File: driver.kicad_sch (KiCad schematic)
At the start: 7 parts, among them J1 Conn_01x02_Pin, J2 Conn_01x02_Pin, U2 DRV8847SPWR

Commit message: patch: mark unused pins
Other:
- title: (none) -> HapticDriver
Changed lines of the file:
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@@
 	(generator_version "7.99")
 	(paper "A4")
+	(title_block
+		(title "HapticDriver")
+		(rev "v0.1")
+	)
 	(junction
 		(at 160.02 114.3)

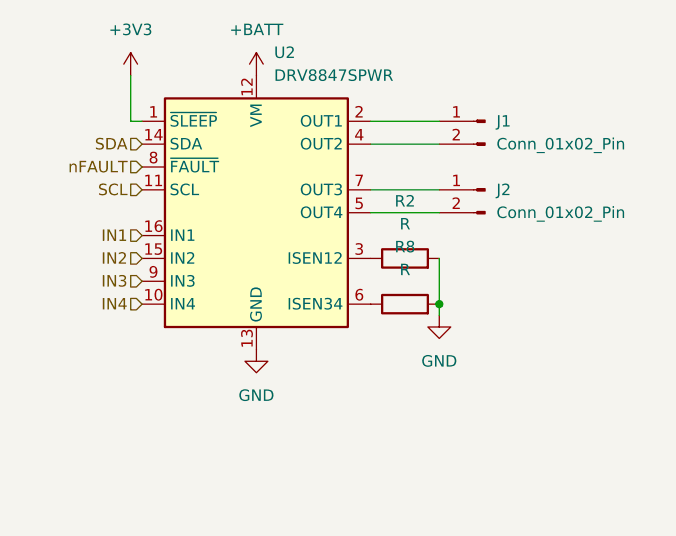
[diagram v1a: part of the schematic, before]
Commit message: patch: specify value of sense resistor
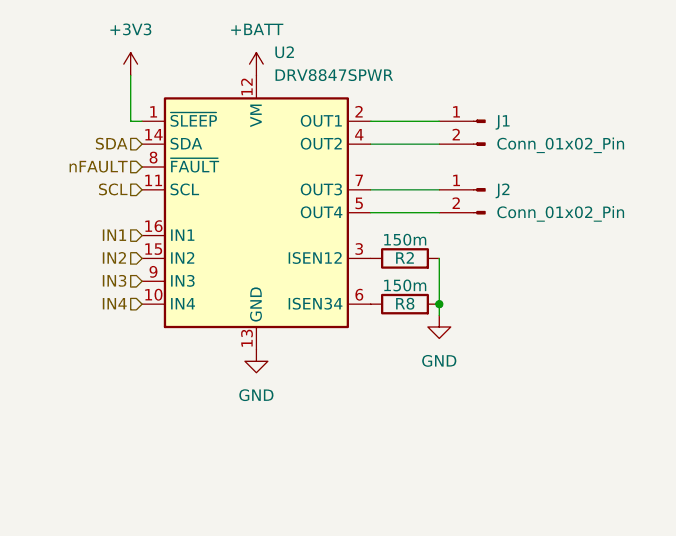
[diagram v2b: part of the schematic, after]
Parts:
- R2, R8: value R -> 150m
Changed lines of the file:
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@@
 		(on_board yes)
 		(dnp no)
-		(fields_autoplaced yes)
 		(property "Reference" "R2"
-			(at 156.21 102.87 90)
+			(at 156.21 109.22 90)
 			(effects
 				(font
@@
 			)
 		)
-		(property "Value" "R"
-			(at 156.21 105.41 90)
+		(property "Value" "150m"
+			(at 156.21 107.188 90)
 			(effects
 				(font
@@
 		(on_board yes)
 		(dnp no)
-		(fields_autoplaced yes)
 		(property "Reference" "R8"
-			(at 156.21 107.95 90)
+			(at 156.21 114.3 90)
 			(effects
 				(font
@@
 			)
 		)
-		(property "Value" "R"
-			(at 156.21 110.49 90)
+		(property "Value" "150m"
+			(at 156.21 112.268 90)
 			(effects
 				(font

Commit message: feat: major redesign with better driver and audio, partial routing
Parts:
- removed C2: 10uF, Capacitor_THT:CP_Radial_D5.0mm_P2.50mm, symbol Device:C_Polarized
- removed J1, J2: Conn_01x02_Pin, Connector_PinHeader_2.54mm:PinHeader_1x02_P2.54mm_Vertical, symbol Connector:Conn_01x02_Pin
- removed R2, R8: 150m, Resistor_SMD:R_1210_3225Metric_Pad1.30x2.65mm_HandSolder, symbol Device:R
- removed U2: DRV8847SPWR, Package_SO:TSSOP-16_4.4x5mm_P0.65mm, symbol Driver_Motor:DRV8847SPWR
- added C2, C5: 0.1uF, Capacitor_SMD:C_0603_1608Metric, symbol Device:C
- added C22: 1uF, Capacitor_SMD:C_0603_1608Metric, symbol Device:C
- added U12: DRV8912QPWPRQ1, Ti:PWP0024N_N, symbol DRV8912:DRV8912QPWPRQ1
- C1: footprint Capacitor_THT:C_Disc_D3.8mm_W2.6mm_P2.50mm -> Capacitor_SMD:C_0603_1608Metric
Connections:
- net +3V3: now also C2.1, C5.1, U12.6 (VDD)
- net +BATT: now also C22.1, U12.16 (VM), U12.21 (VM)
- net GND: now also C2.2, C22.2, C5.2, U12.1 (GND), U12.13 (GND), U12.24 (GND), U12.25 (GND)
- net nFAULT: now also U12.12 (FAULT_N)
- new net SCK: U12.20 (SCLK)
- new net SIN: U12.5 (SDI)
- new net SOUT: U12.7 (SDO)
- new net nCS: U12.19 (SCS_N)
- new net nSLEEP: U12.8 (SLEEP_N)

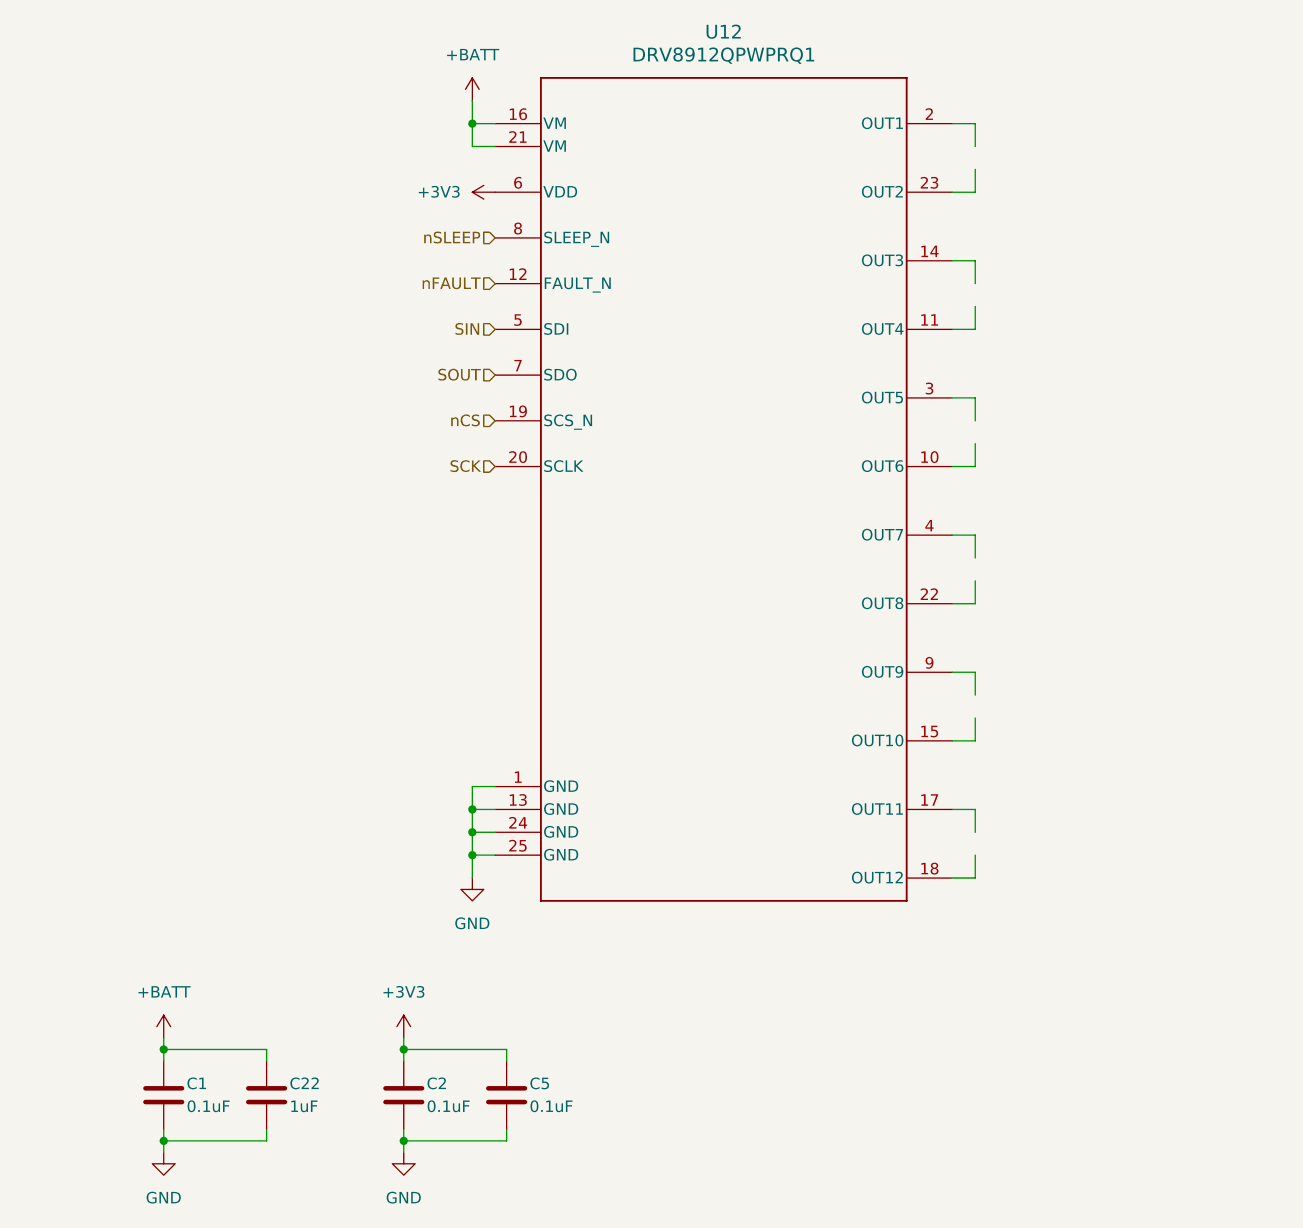
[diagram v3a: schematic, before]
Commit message: feat: full reroute with max22200 driver
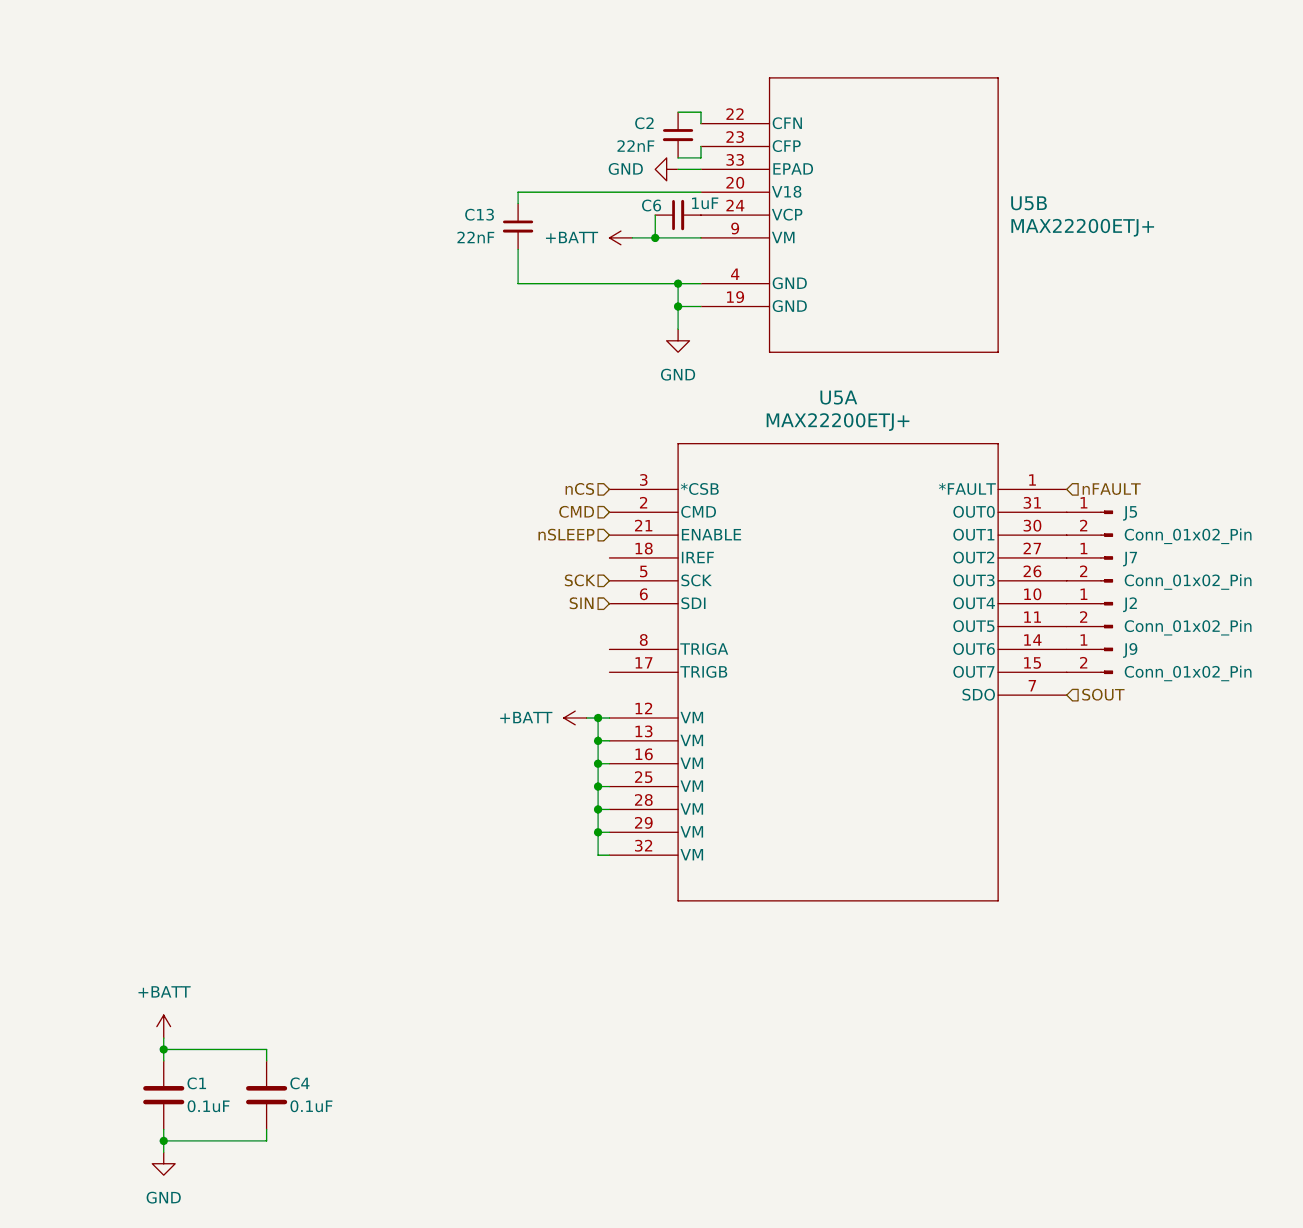
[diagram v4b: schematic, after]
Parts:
- removed C2, C5: 0.1uF, Capacitor_SMD:C_0603_1608Metric, symbol Device:C
- removed C22: 1uF, Capacitor_SMD:C_0603_1608Metric, symbol Device:C
- removed U12: DRV8912QPWPRQ1, Ti:PWP0024N_N, symbol DRV8912:DRV8912QPWPRQ1
- added C13, C2: 22nF, Capacitor_SMD:C_0402_1005Metric, symbol Device:C_Small
- added C4: 0.1uF, Capacitor_SMD:C_0603_1608Metric, symbol Device:C
- added C6: 1uF, Capacitor_SMD:C_0402_1005Metric, symbol Device:C_Small
- added J2, J5, J7, J9: Conn_01x02_Pin, SolderWires:SolderWire_1x02, symbol Connector:Conn_01x02_Pin
- added U5: MAX22200ETJ+, AnalogDevices:21-0140AK_T3255_8C_MXM, symbol max22200:MAX22200ETJ+
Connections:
- net +BATT: now also C4.1, C6.1, U5.12 (VM), U5.13 (VM), U5.16 (VM), U5.25 (VM), U5.28 (VM), U5.29 (VM), U5.32 (VM), U5.9 (VM)
- net GND: now also C13.2, C4.2, U5.19 (GND), U5.33 (EPAD), U5.4 (GND)
- net SCK: now also U5.5 (SCK)
- net SIN: now also U5.6 (SDI)
- net SOUT: now also U5.7 (SDO)
- net nCS: now also U5.3 (*CSB)
- net nFAULT: now also U5.1 (*FAULT)
- net nSLEEP: now also U5.21 (ENABLE)
- new net: J2.1 (Pin_1), U5.10 (OUT4)
- new net: J2.2 (Pin_2), U5.11 (OUT5)
- new net: J9.1 (Pin_1), U5.14 (OUT6)
- new net: J9.2 (Pin_2), U5.15 (OUT7)
- new net: J7.2 (Pin_2), U5.26 (OUT3)
- new net: J7.1 (Pin_1), U5.27 (OUT2)
- new net: J5.2 (Pin_2), U5.30 (OUT1)
- new net: J5.1 (Pin_1), U5.31 (OUT0)
- new net: C2.1, U5.22 (CFN)
- new net: C2.2, U5.23 (CFP)
- new net: C13.1, U5.20 (V18)
- new net: C6.2, U5.24 (VCP)
- new net CMD: U5.2 (CMD)

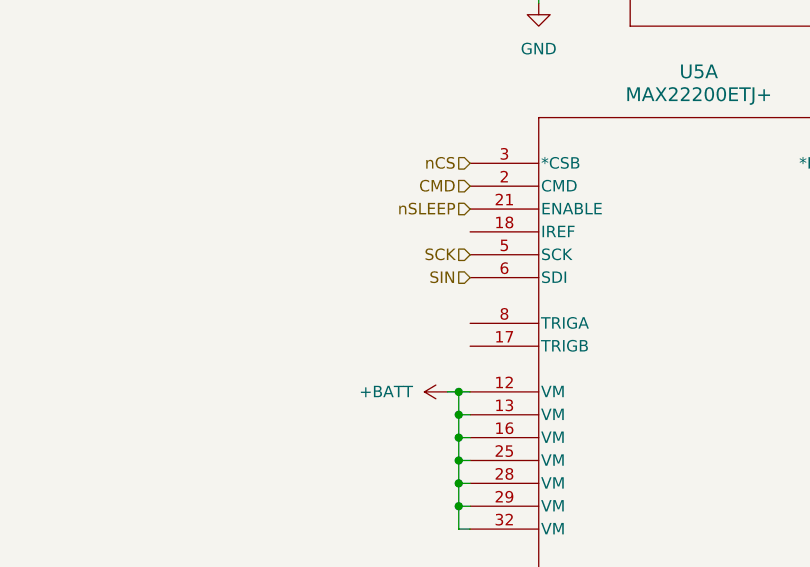
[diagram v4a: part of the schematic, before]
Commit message: feat: fully routed v2 design
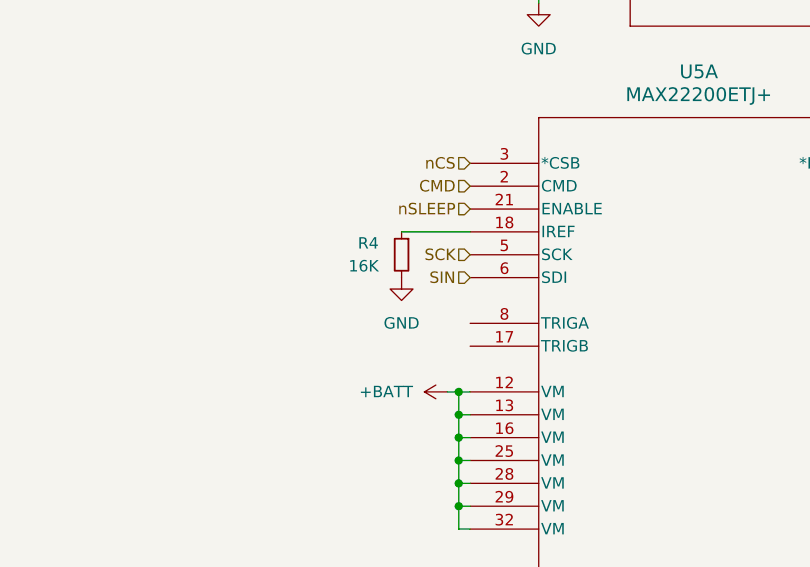
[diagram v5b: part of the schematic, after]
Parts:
- added R4: 16K, Resistor_SMD:R_0402_1005Metric, symbol Device:R_Small
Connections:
- net GND: now also R4.2
- net at U5.18 (IREF): now also R4.1
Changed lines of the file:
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@@
+	(wire
+		(pts
+			(xy 120.65 101.6) (xy 128.27 101.6)
+		)
+		(stroke
+			(width 0)
+			(type default)
+		)
+	)
 	(wire
 		(pts
@@
 	)
 	(symbol
+		(lib_id "Device:R_Small")
+		(at 120.65 104.14 0)
+		(mirror y)
+		(unit 1)
+		(exclude_from_sim no)
+		(in_bom yes)
+		(on_board yes)
+		(dnp no)
+		(property "Reference" "R4"
+			(at 118.11 102.8699 0)
+			(effects
+				(font
+					(size 1.27 1.27)
+				)
+				(justify left)
+			)
+		)
+		(property "Value" "16K"
+			(at 118.11 105.4099 0)
+			(effects
+				(font
+					(size 1.27 1.27)
+				)
+				(justify left)
+			)
+		)
+		(property "Footprint" "Resistor_SMD:R_0402_1005Metric"
+			(at 120.65 104.14 0)
+			(effects
+				(font
+					(size 1.27 1.27)
+				)
+				(hide yes)
+			)
+		)
+		(property "Datasheet" "~"
+			(at 120.65 104.14 0)
+			(effects
+				(font
+					(size 1.27 1.27)
+				)
+				(hide yes)
+			)
+		)
+		(property "Description" "Resistor, small symbol"
+			(at 120.65 104.14 0)
+			(effects
+				(font
+					(size 1.27 1.27)
+				)
+				(hide yes)
+			)
+		)
+		(property "Part" "C543609"
+			(at 120.65 104.14 0)
+			(effects
+				(font
+					(size 1.27 1.27)
+				)
+				(hide yes)
+			)
+		)
+		(pin "1"
+		)
+		(pin "2"
+		)
+		(instances
+			(project "HapticDriver"
+				(path "/89c84321-602a-4eb8-8dad-33289e154cd9/e20c0ed8-6e50-4d86-9157-9aa2e157c95b"
+					(reference "R4")
+					(unit 1)
+				)
+				(path "/89c84321-602a-4eb8-8dad-33289e154cd9/2c530d14-1ef3-4f14-904d-5a3fc613eb72"
+					(reference "R5")
+					(unit 1)
+				)
+			)
+		)
+	)
+	(symbol
 		(lib_id "Connector:Conn_01x02_Pin")
 		(at 184.15 101.6 0)
@@
 					(unit 1)
 				)
+			)
+		)
+	)
+	(symbol
+		(lib_id "power:GND")
+		(at 120.65 106.68 0)
+		(unit 1)
+		(exclude_from_sim no)
+		(in_bom yes)
+		(on_board yes)
+		(dnp no)
+		(fields_autoplaced yes)
+		(property "Reference" "#PWR020"
+			(at 120.65 113.03 0)
+			(effects
+				(font
+					(size 1.27 1.27)
+				)
+				(hide yes)
+			)
+		)
+		(property "Value" "GND"
+			(at 120.65 111.76 0)
+			(effects
+				(font
+					(size 1.27 1.27)
+				)
+			)
+		)
+		(property "Footprint" ""
+			(at 120.65 106.68 0)
+			(effects
+				(font
+					(size 1.27 1.27)
+				)
+				(hide yes)
+			)
+		)
+		(property "Datasheet" ""
+			(at 120.65 106.68 0)
+			(effects
+				(font
+					(size 1.27 1.27)
+				)
+				(hide yes)
+			)
+		)
+		(property "Description" ""
+			(at 120.65 106.68 0)
+			(effects
+				(font
+					(size 1.27 1.27)
+				)
+				(hide yes)
+			)
+		)
+		(pin "1"
+		)
+		(instances
+			(project "HapticDriver"
+				(path "/89c84321-602a-4eb8-8dad-33289e154cd9/e20c0ed8-6e50-4d86-9157-9aa2e157c95b"
+					(reference "#PWR020")
+					(unit 1)
+				)
+				(path "/89c84321-602a-4eb8-8dad-33289e154cd9/2c530d14-1ef3-4f14-904d-5a3fc613eb72"
+					(reference "#PWR032")
+					(unit 1)
+				)

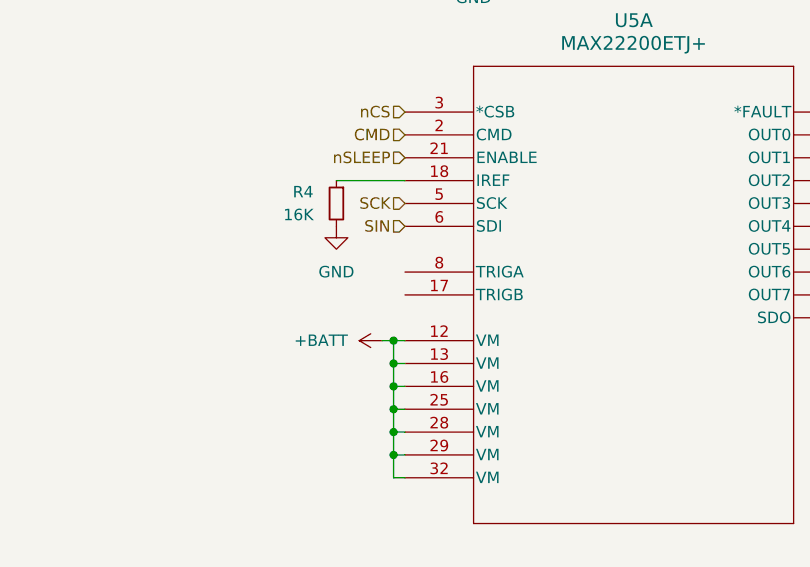
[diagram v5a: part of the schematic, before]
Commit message: feat: battery level measurement resistors
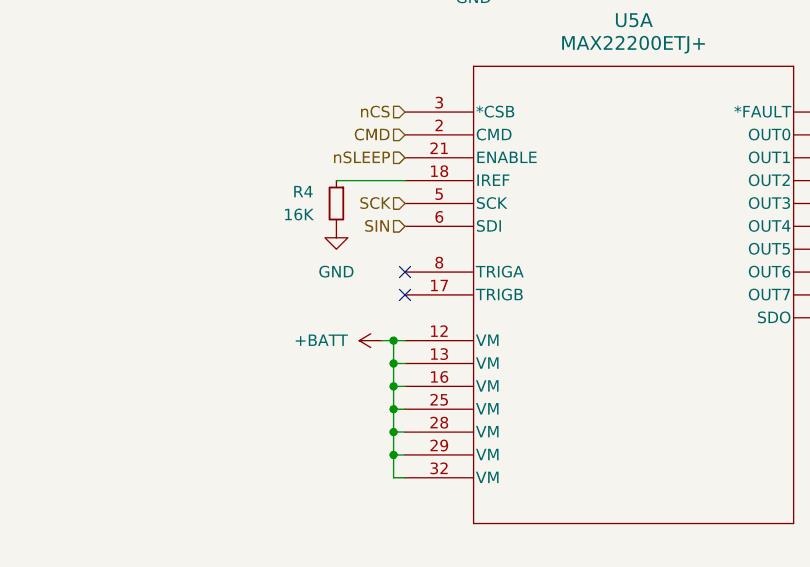
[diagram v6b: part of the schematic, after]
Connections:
- no-connect marks 0 -> 2
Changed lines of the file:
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@@
 		(color 0 0 0 0)
+	)
+	(no_connect
+		(at 128.27 111.76)
+	)
+	(no_connect
+		(at 128.27 114.3)
 	)
 	(wire

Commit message: feat: populate all jlcpcb part#
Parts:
- C1, C4: Part (none) -> C14663
- C13: Part C368595 -> C1532
- C2: Part C524553 -> C1532
- C6: Part C361059 -> C52923
- U5: Part (none) -> C2845158
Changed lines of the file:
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@@
+			)
+		)
+		(property "Part" "C2845158"
+			(at 128.27 93.98 0)
+			(effects
+				(font
+					(size 1.27 1.27)
+				)
+				(hide yes)
 			)
 		)
@@
 			)
 		)
-		(property "Part" "C524553"
+		(property "Part" "C1532"
 			(at 135.89 54.61 0)
 			(effects
@@
 			)
 		)
+		(property "Part" "C14663"
+			(at 78.74 161.29 0)
+			(effects
+				(font
+					(size 1.27 1.27)
+				)
+				(hide yes)
+			)
+		)
 		(pin "1"
 		)
@@
 			)
 		)
+		(property "Part" "C2845158"
+			(at 138.43 53.34 0)
+			(effects
+				(font
+					(size 1.27 1.27)
+				)
+				(hide yes)
+			)
+		)
 		(pin "27"
 		)
@@
 			)
 		)
-		(property "Part" "C368595"
+		(property "Part" "C1532"
 			(at 118.11 64.77 0)
 			(effects
@@
 			)
 		)
-		(property "Part" "C361059"
+		(property "Part" "C52923"
 			(at 135.89 63.5 0)
 			(effects
@@
 			(at 90.17 161.29 0)
 			(effects
+				(font
+					(size 1.27 1.27)
+				)
+				(hide yes)
+			)
+		)
+		(property "Part" "C14663"
+			(at 90.17 161.29 0)
+			(effects
